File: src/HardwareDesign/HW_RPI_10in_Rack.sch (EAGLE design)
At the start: 12 parts, among them IC1 RT9742NGV, J1 10164227-1001A1RLF, J2 10164227-1001A1RLF, J3 692141030100, J4 685119136923, J5 685119136923

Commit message: schematic-baseline finished
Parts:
- added 2230, 2242, 2260, 2280: M2 x 1mm, Wurth_Assembly_WA-SMSI:WA-SMSI_9774XXX243_9774010243
- added BT1: 79523141, Battery Holder:79523141
- added C10, C11, C12, C20, C5, C9: 100nF, ds_passive:C0402
- added C13: 4.7nF, ds_passive:C0402
- added C14, C15, C16, C17, C18, C19, C6, C7: 10uF, ds_passive:C0805
- added C8: 100uF, rcl:CPOL-EU153CLV-0505
- added D1, D2: TPD4EUSB30, ds_ic_peripherals:TPD4EUSB30
- added ETH1: (no value), ds_con:MAGJACK
- added IC2: AP22653W6, ds_ic_peripherals:AP22653W6
- added IC3: 74LVC1G07, ds_ic_logic:74LVC1G07
- added IC4: RT9742NGV, ds_ic_peripherals:RT9742NGV
- added IC5: (no value), ds_ic_vreg:AP3441SHE-7B
- added JP1, JP3: (no value), jumper:JP2Q
- added JP2: (no value), jumper:JP7Q
- added L1: (no value), rcl:L-USL5038P
- added LED1: Green, led:LEDCHIPLED_0805
- added LED2: (no value), led:LEDCHIPLED_0805
- added R10: (no value), ds_passive:R0402
- added R11: 100K 1%, ds_passive:R0402
- added R12: 10K 1%, ds_passive:R0402
- added R13, R3, R4: 2.2K 1%, ds_passive:R0402
- added R2: 15K 1%, ds_passive:R0402
- added R5: 1K, ds_passive:R0402
- added R6: 0R, ds_passive:R0402
- added R7: DNI, ds_passive:R0402
- added R8, R9: 470R, ds_passive:R0402
- added S1: (no value), adafruit:31-XX
- added SV1: (no value), con-lstb:MA04-1
- added SV2: (no value), con-lstb:MA20-2
- added U$1: MICROSD, adafruit:MICROSD
- added U$2: M.2, ds_con:M.2
- added X1: ASEK-32.768KHz-LRT, crystal-geyer_V1_0:KXO-PXO/XO-V96
- IC1: value RT9742NGV -> (none); device ds_ic_peripherals:RT9742NGV -> ds_ic_peripherals:RT9742GGJ5
- R1: value 2.2k 1% -> 2.2K 1%
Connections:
- new net EEPROM_WP: JP2.4
- new net M2_3V3: C12.1, C13.1, C14.1, C15.1, C16.1, C17.1, L1.2, R12.1, U$2.VCC1, U$2.VCC2, U$2.VCC3, U$2.VCC4, U$2.VCC5, U$2.VCC6, U$2.VCC7, U$2.VCC8, U$2.VCC9, X1.TS, X1.VDD
- new net N$1: IC2.ILIM, R2.1
- new net N$10: C13.2, IC5.FB, R12.2, R13.1
- new net N$11: U$2.SUSCLK, X1.OUT
- new net N$2: LED1.C, R5.1
- new net N$3: IC3.Y, R5.2
- new net N$4: C11.1, ETH1.P1, ETH1.P10
- new net N$5: ETH1.P13, R9.1
- new net N$6: R10.2, U$2.DA5/!DSS!/!LED1
- new net N$7: LED2.C, R10.1
- new net N$8: ETH1.P12, R8.2
- new net N$9: IC5.LX, L1.1
- new net SCL1: JP1.2, R4.2
- new net SDA1: JP1.4, R3.2
- new net SD_PWR: C10.1, IC1.OUT, U$1.VDD
- new net TACHO: SV1.1
- new net USBOTG: JP2.10
- net +1V8: now also R7.1
- net +3V3: now also C9.1, ETH1.P11, ETH1.P14, IC1.IN, IC3.VCC, LED1.A, LED2.A, R6.1, SV2.1, SV2.17
- net +5V: now also C18.1, C19.1, C20.1, C5.1, IC2.IN, IC4.IN, IC5.VIN, SV1.4, SV2.2, SV2.4; no longer IC1.IN
- net BT_NDIS: now also JP3.3
- net ETH_LEDG: now also R8.1
- net ETH_LEDY: now also R9.2
- net GND: now also 2230.1, 2242.1, 2260.1, 2280.1, BT1.-, C10.2, C11.2, C12.2, C14.2, C15.2, C16.2, C17.2, C18.2, C19.2, C20.2, C5.2, C6.2, C7.2, C8.-, C9.2, D1.GND, D2.GND, ETH1.SHIELD, IC2.GND, IC3.GND, IC4.GND, IC5.PGND, IC5.SGND, JP2.1, JP2.11, JP2.13, JP2.3, JP2.5, JP2.7, JP2.9, JP3.2, JP3.4, R11.2, R13.2, R2.2, S1.S, SV1.2, SV2.14, SV2.20, SV2.25, SV2.30, SV2.34, SV2.39, SV2.6, SV2.9, U$1.GND, U$1.GND1, U$1.VSS, U$2.GND1, U$2.GND10, U$2.GND11, U$2.GND12, U$2.GND13, U$2.GND14, U$2.GND2, U$2.GND3, U$2.GND4, U$2.GND5, U$2.GND6, U$2.GND7, U$2.GND8, U$2.GND9, U$2.S1, U$2.S2, X1.GND
- net GPIO10: now also SV2.19
- net GPIO11: now also SV2.23
- net GPIO12: now also SV2.32
- net GPIO13: now also SV2.33
- net GPIO14: now also SV2.8
- net GPIO15: now also SV2.10
- net GPIO16: now also SV2.36
- net GPIO17: now also SV2.11
- net GPIO18: now also SV2.12
- net GPIO19: now also SV2.35
- net GPIO2: now also SV2.3
- net GPIO20: now also SV2.38
- net GPIO21: now also SV2.40
- net GPIO22: now also SV2.15
- net GPIO23: now also SV2.16
- net GPIO24: now also SV2.18
- net GPIO25: now also SV2.22
- net GPIO26: now also SV2.37
- net GPIO27: now also SV2.13
- net GPIO3: now also SV2.5
- net GPIO4: now also SV2.7
- net GPIO5: now also SV2.29
- net GPIO6: now also SV2.31
- net GPIO7: now also SV2.26
- net GPIO8: now also SV2.24
- net GPIO9: now also SV2.21
- net GPIO_VREF: now also R3.1, R4.1, R6.2, R7.2
- net HDMI_5V: now also IC4.OUT; no longer IC1.OUT
- net ID_SC: now also JP1.1, SV2.28
- net ID_SD: now also JP1.3, SV2.27
- net NPWR_LED: now also IC3.A
- net NRPIBOOT: now also JP2.2
- net PCIE_CLK_N: now also U$2.REFCLK_N
- net PCIE_CLK_P: now also U$2.REFCLK_P
- net PCIE_NCLKREQ: now also U$2.!CLKREQ
- net PCIE_NRST: now also U$2.!PERST
- net PCIE_NWAKE: now also U$2.!PEWAKE
- net PCIE_PWR_EN: now also IC5.EN, R11.1
- net PCIE_RX_N: now also U$2.PET_P0
- net PCIE_RX_P: now also U$2.PET_N0
- net PCIE_TX_N: now also U$2.PER_P0
- net PCIE_TX_P: now also U$2.PER_N0
- net PMIC_ENABLE: now also JP2.12
- net PWM: now also SV1.3
- net PWR_BUT: now also JP2.14, S1.P
- net SD_CLK: now also U$1.SCLK
- net SD_CMD: now also U$1.DATA_IN
- net SD_DAT0: now also U$1.DATA_OUT
- net SD_DAT1: now also U$1.DAT1
- net SD_DAT2: now also U$1.DAT2
- net SD_DAT3: now also U$1.CS
- net SD_PWR_ON: now also IC1.EN
- net SYNC_OUT: now also JP2.6
- net TRD0_N: now also D2.D1+, ETH1.P3
- net TRD0_P: now also D2.D1-, ETH1.P2
- net TRD1_N: now also D2.D2-, ETH1.P5
- net TRD1_P: now also D2.D2+, ETH1.P4
- net TRD2_N: now also D1.D1+, ETH1.P7
- net TRD2_P: now also D1.D1-, ETH1.P6
- net TRD3_N: now also D1.D2-, ETH1.P9
- net TRD3_P: now also D1.D2+, ETH1.P8
- net VBAT: now also BT1.+
- net VBUS: now also C6.1, C7.1, C8.+, IC2.OUT
- net VBUS_EN: now also IC2.EN
- net WL_NDIS: now also JP3.1
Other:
- note added: "1000 BASE ETHERNET"
- note added: "40-PIN GPIO HEADER"
- note added: "CURRENT LIMIT SWITCH"
- note added: "DPHY1 JUMPERS"
- note added: "FAN CONNECTOR"
- note added: "GPIO VOLTAGE SELECT"
- note added: "JUMPERS"
- note added: "MICRO-SD SOCKET"
- note added: "PCIE POWER SUPPLY"
- note added: "PCIE-M.2 M-KEY CONNECTOR"
- note added: "POWER BUTTON AND LED"
- note added: "RF DISABLE"
- note added: "RTC BATTERY"
- moved on the sheet: C1, C2, C3, C4, J3USBA, J3USBB, J4, J5, R1, USB1

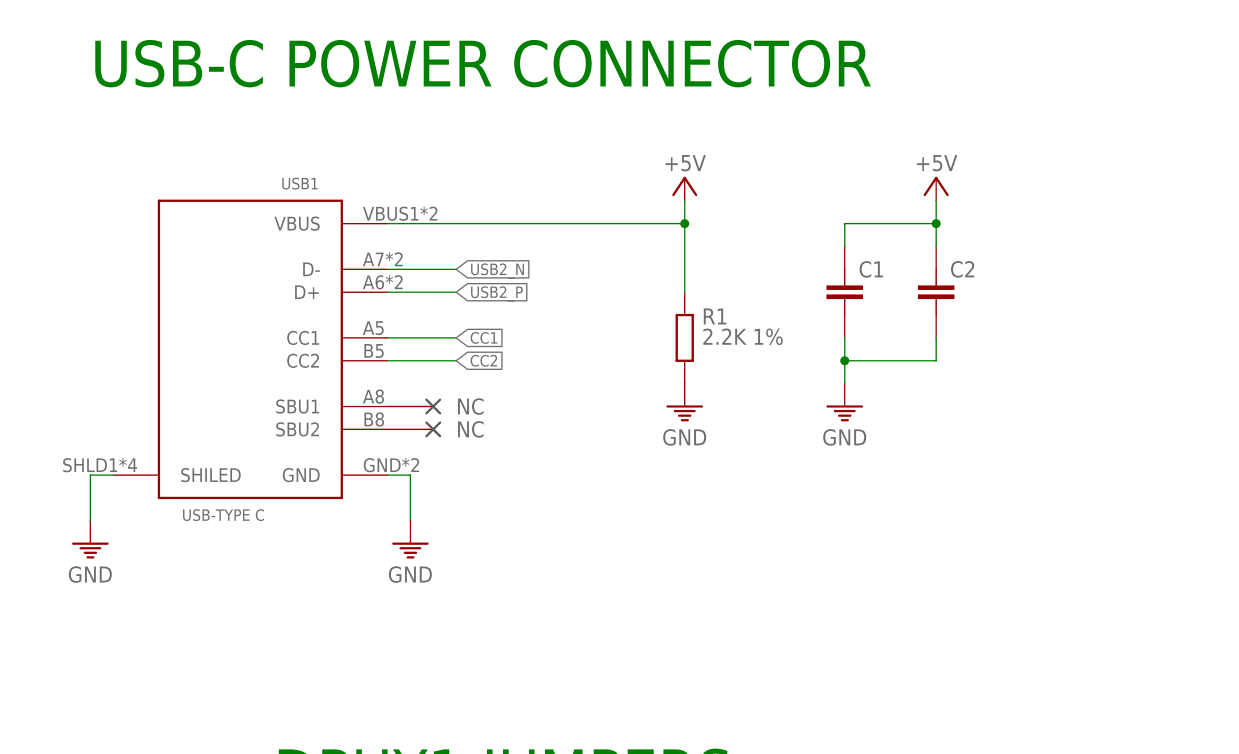
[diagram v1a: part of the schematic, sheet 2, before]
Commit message: add DAQ to design
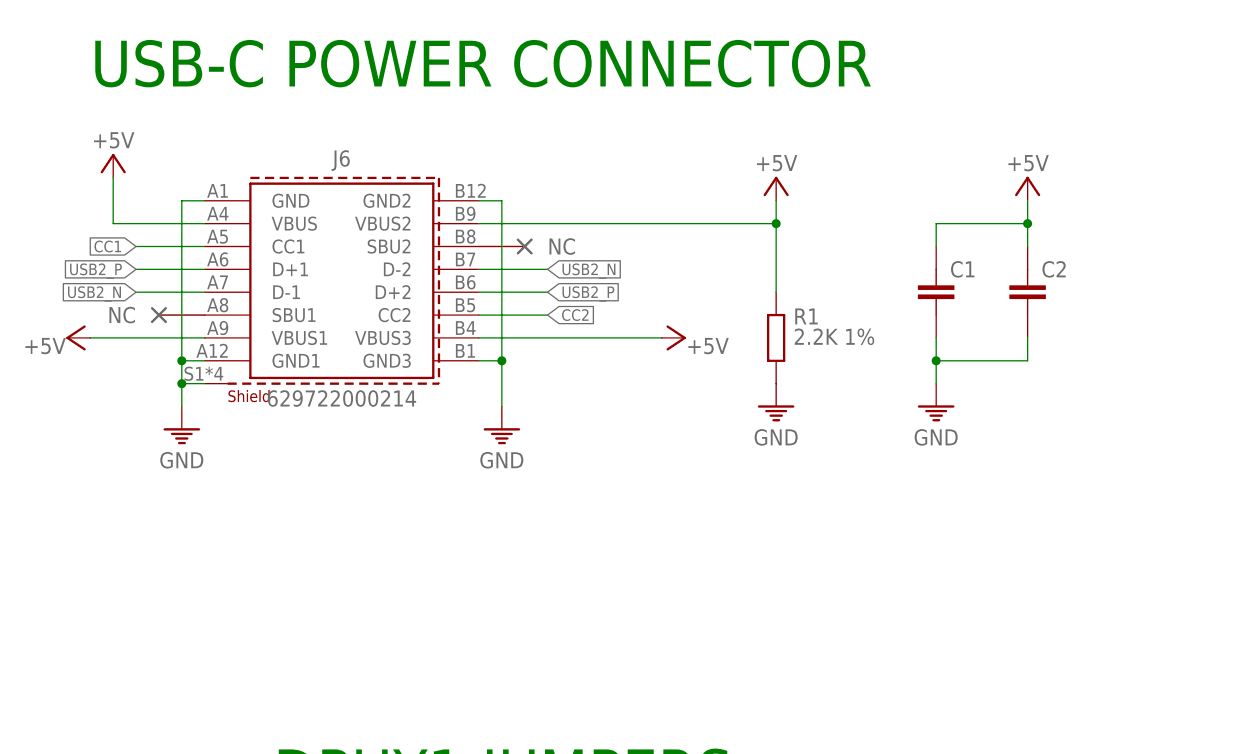
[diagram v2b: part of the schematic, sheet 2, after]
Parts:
- removed USB1: (no value), ds_con:USB_C
- added J6: 629722000214, Wurth_Connectors_WR-USB:629722000214
- added U$3: M.2, ds_con:M.2
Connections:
- removed net TACH0: J2.16
- net +5V: now also J6.VBUS, J6.VBUS1, J6.VBUS2, J6.VBUS3; no longer USB1.VBUS
- net CC1: now also J6.CC1; no longer USB1.CC1
- net CC2: now also J6.CC2; no longer USB1.CC2
- net GND: now also J6.GND, J6.GND1, J6.GND2, J6.GND3, J6.SHIELD; no longer USB1.GND, USB1.SHILED
- net TACHO: now also J2.16
- net TRD0_N: now also D2.D1-; no longer D2.D1+
- net TRD0_P: now also D2.D1+; no longer D2.D1-
- net TRD1_N: now also D2.D2+; no longer D2.D2-
- net TRD1_P: now also D2.D2-; no longer D2.D2+
- net TRD2_N: now also D1.D1-; no longer D1.D1+
- net TRD2_P: now also D1.D1+; no longer D1.D1-
- net TRD3_N: now also D1.D2+; no longer D1.D2-
- net TRD3_P: now also D1.D2-; no longer D1.D2+
- net USB2_N: now also J6.D-1, J6.D-2; no longer USB1.D-
- net USB2_P: now also J6.D+1, J6.D+2; no longer USB1.D+
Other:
- moved on the sheet: C1, C2, IC5, R1
